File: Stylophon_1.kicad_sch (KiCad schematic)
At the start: 71 parts, among them J1 Conn_01x02_Socket, J2 +, J3 -, J4 Stylus, SW1 On/Off, SW2 Vibrato, T1 BC846, T2 BC846, U1 NE555D

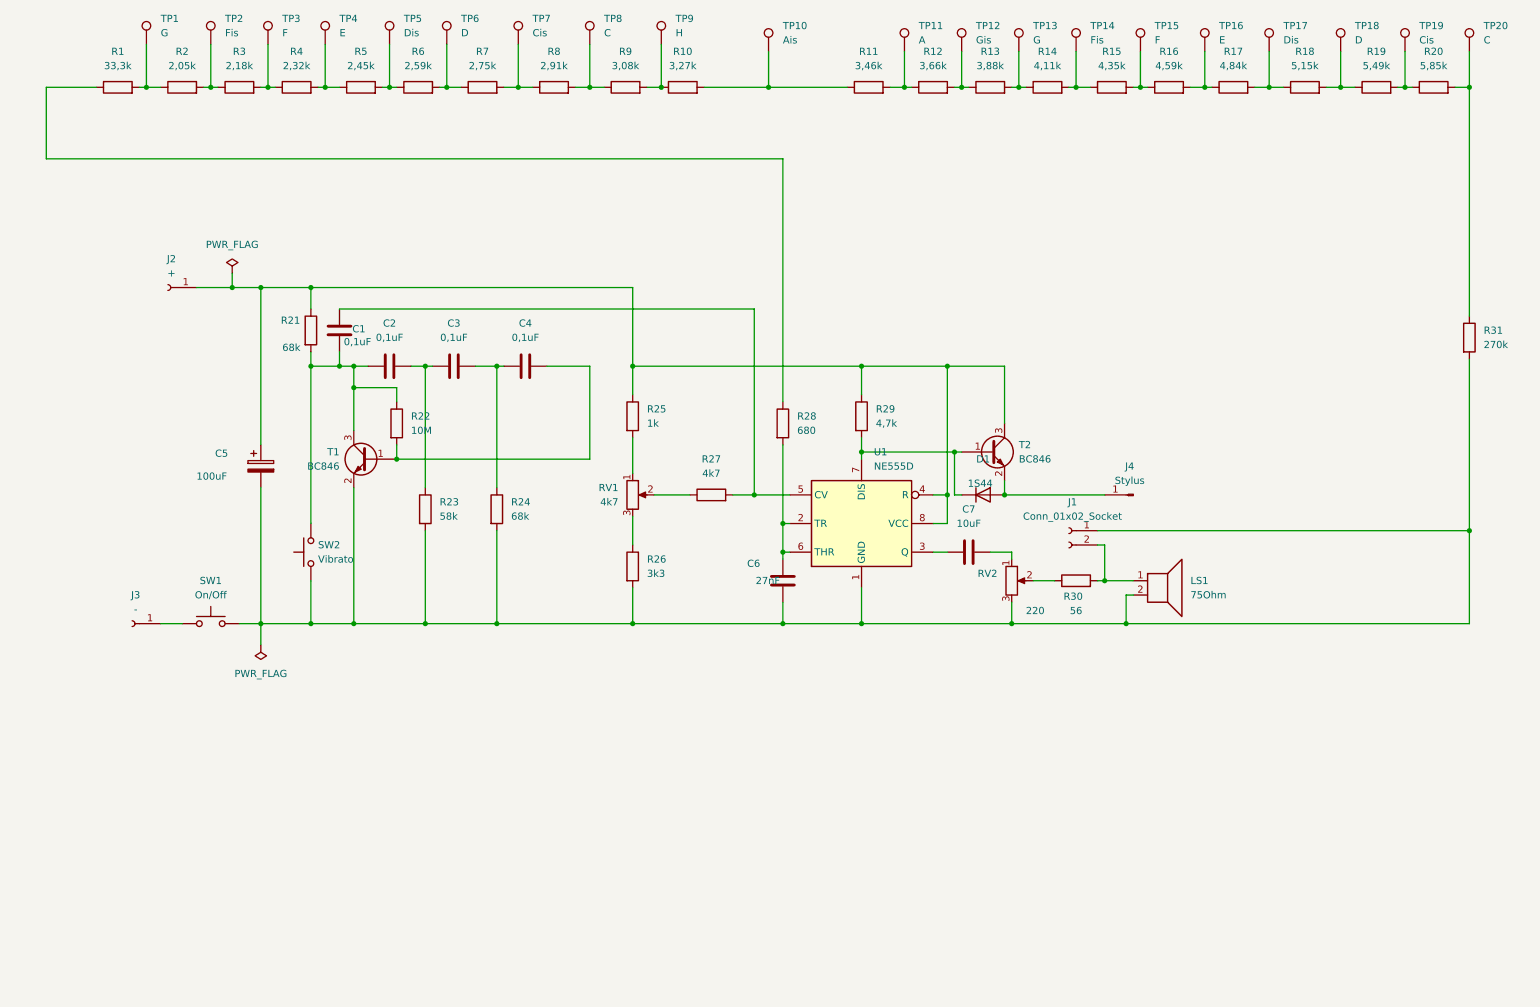
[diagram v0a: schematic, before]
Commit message: Updated Component Values
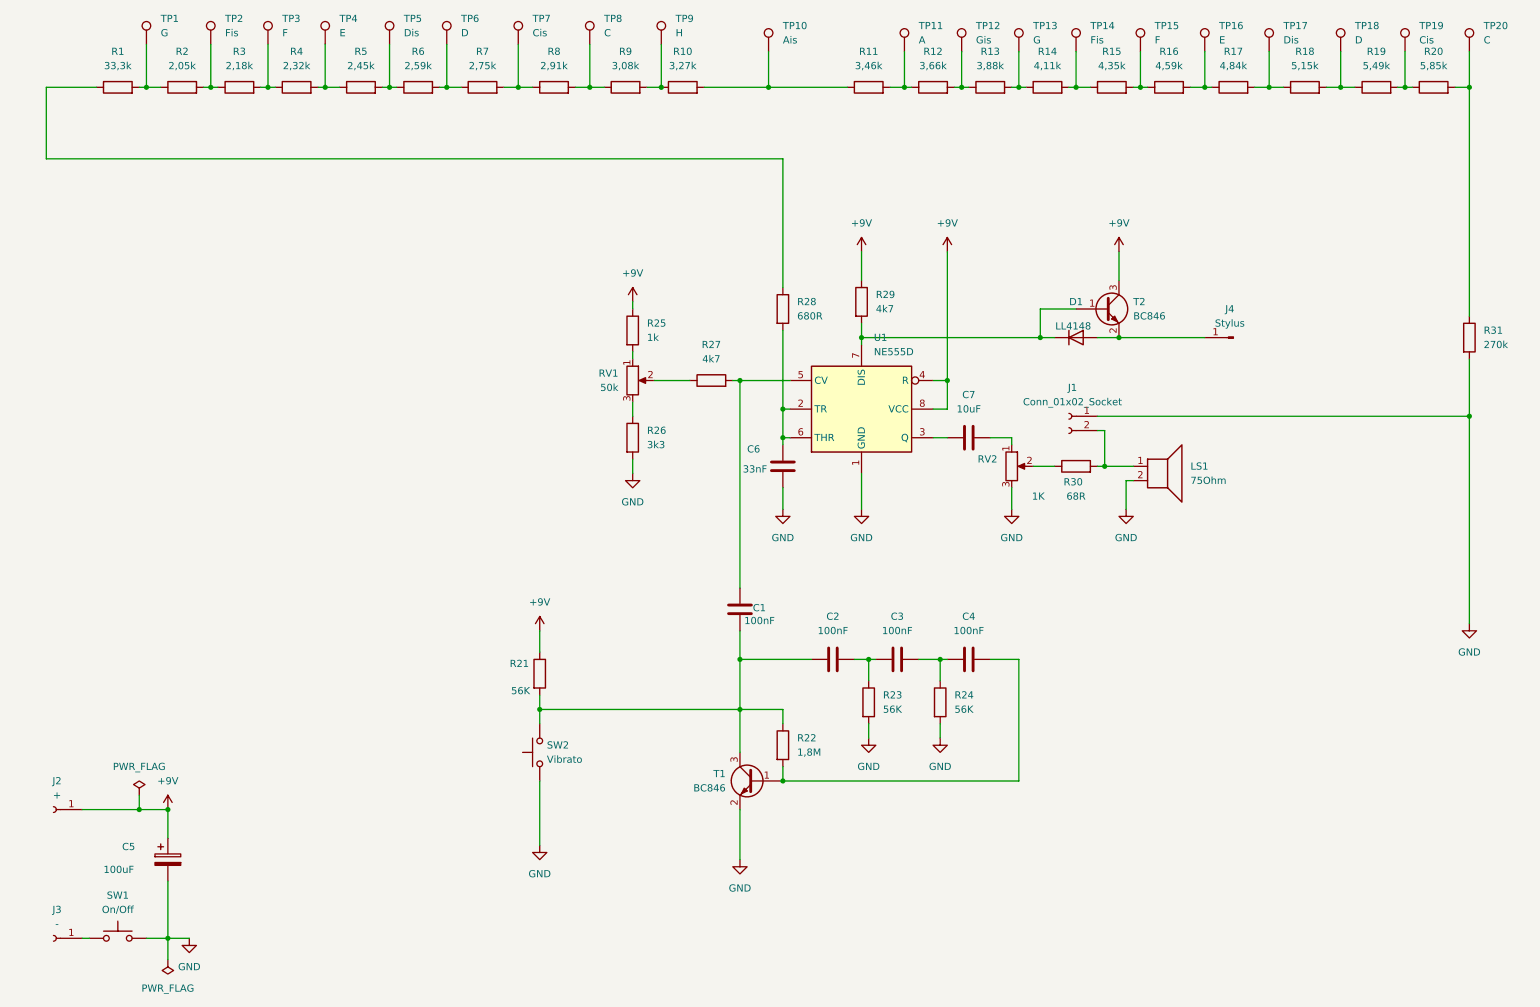
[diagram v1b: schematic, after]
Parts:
- C1, C2, C3, C4: value 0,1uF -> 100nF
- C6: value 27nF -> 33nF
- D1: value 1S44 -> LL4148
- R21, R24: value 68k -> 56K
- R22: value 10M -> 1,8M
- R23: value 58k -> 56K
- R28: value 680 -> 680R
- R29: value 4,7k -> 4k7
- R30: value 56 -> 68R
- RV1: value 4k7 -> 50k
- RV2: value 220 -> 1K
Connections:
- net +9V: now reaches C5.1, J2.1 (Pin_1), R21.1, R25.1, R29.1, T2.3 (C), U1.4 (R), U1.8 (VCC)
- net GND: now reaches C5.2, C6.2, J1.1 (Pin_1), LS1.2, R23.2, R24.2, R26.2, R31.2, RV2.3, SW1.2, SW2.1, T1.2 (E), U1.1 (GND)
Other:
- moved on the sheet: C1, C2, C3, C4, C5, C6, C7, D1, J1, J2, J3, J4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

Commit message: PCB updated
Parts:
- removed J2: +, Connector_PinHeader_2.00mm:PinHeader_1x01_P2.00mm_Vertical, symbol Connector:Conn_01x01_Socket
- removed J3: -, Connector_PinHeader_2.00mm:PinHeader_1x01_P2.00mm_Vertical, symbol Connector:Conn_01x01_Socket
- added BT1: Battery, Connector_PinHeader_2.54mm:PinHeader_1x02_P2.54mm_Vertical, symbol Device:Battery
- TP1, TP10, TP11, TP12, TP13, TP14, TP15, TP16, TP17, TP18, TP19, TP2, TP20, TP3, TP4, TP5, TP6, TP7, TP8, TP9: footprint TestPoint:TestPoint_Pad_4.0x4.0mm -> Keypads:Keypad_Small
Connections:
- net +9V: now also BT1.1 (+)
- net GND: now also LS1.1, RV2.1; no longer LS1.2, RV2.3
- net 5: now reaches R13.2, R14.1, TP13.1
- net 4,5: now reaches R14.2, R15.1, TP14.1
- net 6,5: now reaches R11.2, R12.1, TP11.1
- net 11: now reaches R3.2, R4.1, TP3.1
- net 10,5: now reaches R4.2, R5.1, TP4.1
- net 3,5: now reaches R16.2, R17.1, TP16.1
- net 6: now reaches R12.2, R13.1, TP12.1
- net 3: now reaches R17.2, R18.1, TP17.1
- net 2: now reaches R18.2, R19.1, TP18.1
- net 1: now reaches R20.2, R31.1, TP20.1
- net at SW1.1: now also BT1.2 (-)
- net 10: now reaches R5.2, R6.1, TP5.1
- net 8,5: now reaches R7.2, R8.1, TP7.1
- net 8: now reaches R8.2, R9.1, TP8.1
- net at C7.2: now also RV2.3; no longer RV2.1
- net at J1.2 (Pin_2), R30.2: now also LS1.2; no longer LS1.1
- net 7,5: now reaches R10.1, R9.2, TP9.1
- net 12: now reaches R1.2, R2.1, TP1.1
- net 11,5: now reaches R2.2, R3.1, TP2.1
- net 4: now reaches R15.2, R16.1, TP15.1
- net 7: now reaches R10.2, R11.1, TP10.1
- net 9: now reaches R6.2, R7.1, TP6.1
- net 1,5: now reaches R19.2, R20.1, TP19.1
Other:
- moved on the sheet: R10, R2, R3, TP2

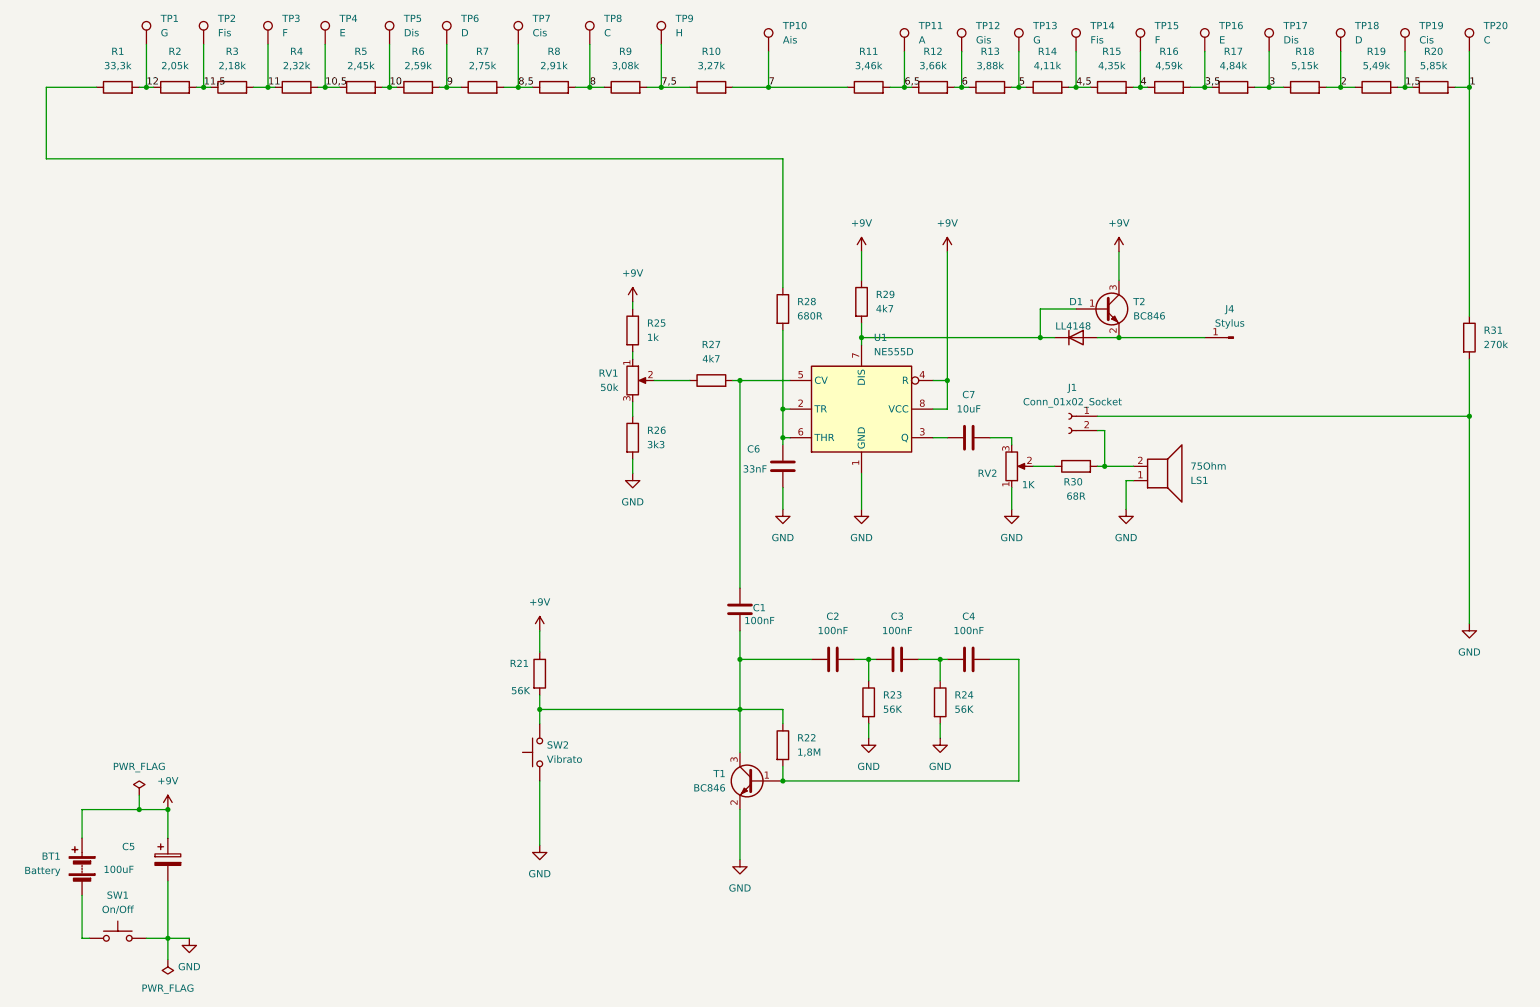
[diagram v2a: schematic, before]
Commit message: Added keys like a real one
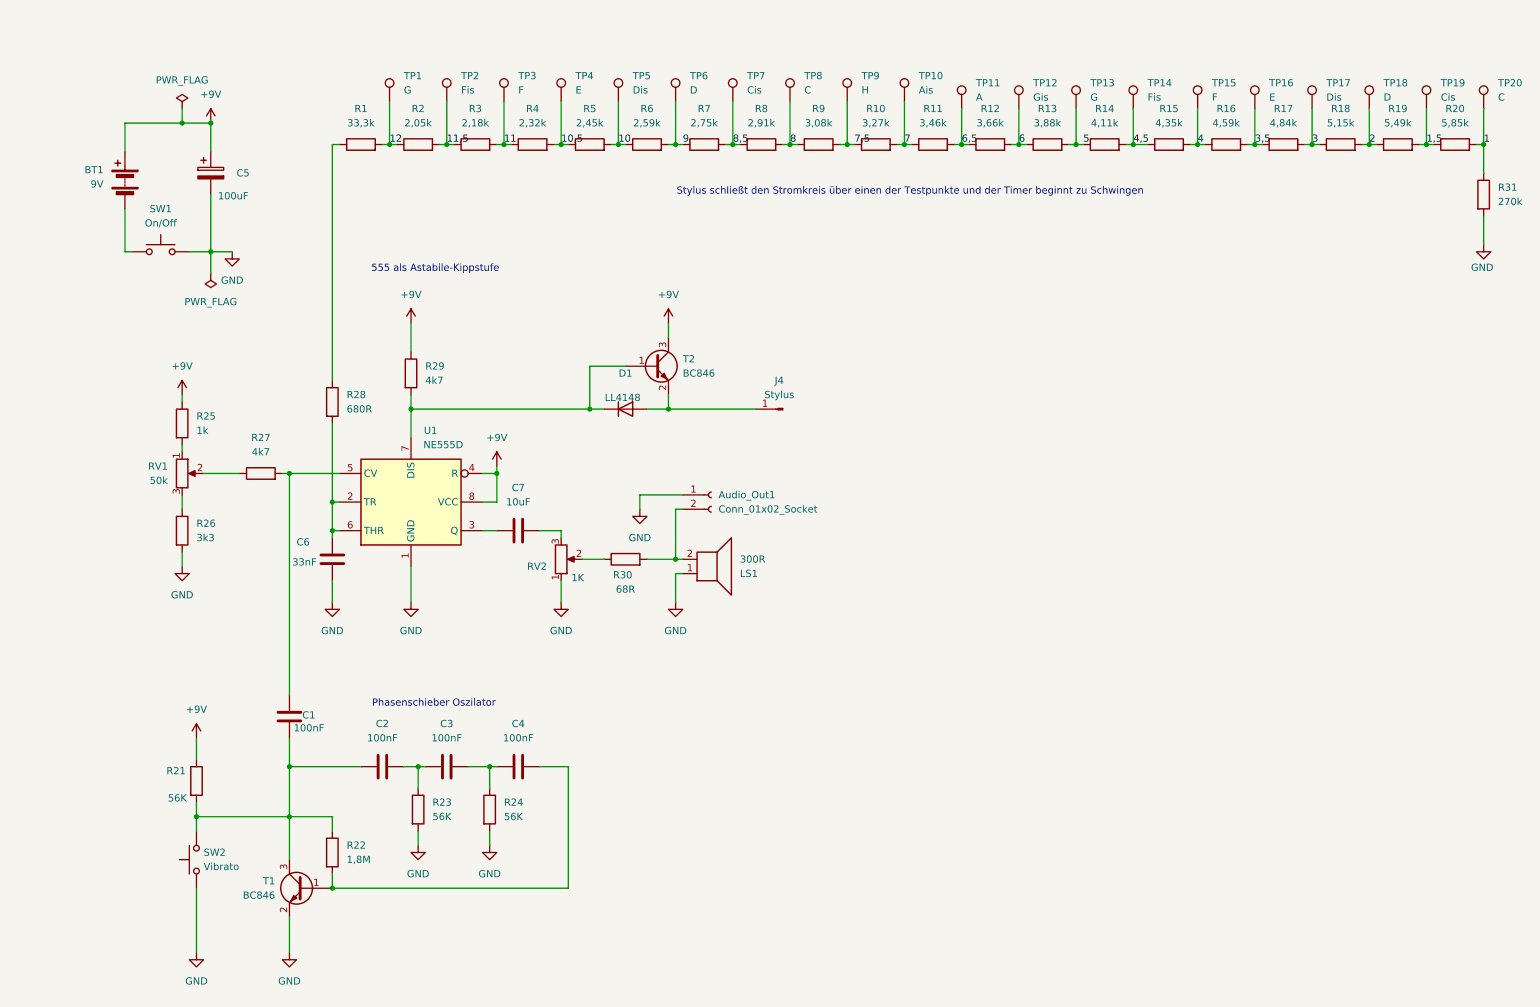
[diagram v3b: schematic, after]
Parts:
- BT1: value Battery -> 9V
- LS1: value 75Ohm -> 300R
- TP1, TP13, TP18, TP6: footprint Keypads:Keypad_Small -> Keypads:Keypad_Right; now left out of the parts list
- TP10, TP11, TP14, TP15, TP16, TP19, TP2, TP3, TP4, TP7, TP8, TP9: now left out of the parts list
- TP12, TP17, TP20, TP5: footprint Keypads:Keypad_Small -> Keypads:Keypad_Left; now left out of the parts list
- renumbered J1 to Audio_Out1
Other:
- note added: "555 als Astabile-Kippstufe"
- note added: "Phasenschieber Oszilator"
- note added: "Stylus schließt den Stromkreis über einen der Testpunkte und der Timer beginnt zu Schwingen"
- moved on the sheet: Audio_Out1, BT1, C1, C2, C3, C4, C5, C6, C7, D1, J4, LS1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

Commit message: VIA stitching & GND Plane QR
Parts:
- added TP21: 9V, TestPoint:TestPoint_Pad_D1.5mm, symbol Connector:TestPoint
- added TP22: GND, TestPoint:TestPoint_Pad_D1.5mm, symbol Connector:TestPoint
- added TP23: Output, TestPoint:TestPoint_Pad_D1.5mm, symbol Connector:TestPoint
- added TP24: Sinus, TestPoint:TestPoint_Pad_D1.5mm, symbol Connector:TestPoint
- added TP25: Batterie, TestPoint:TestPoint_Pad_D1.5mm, symbol Connector:TestPoint
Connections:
- net +9V: now also TP21.1, TP25.1
- net GND: now also TP22.1
- net at C1.1, C2.2, R21.2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: now also TP24.1
- net at C7.1, U1.3 (Q): now also TP23.1
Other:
- note added: "NE555 als Astabile-Kippstufe"
- note removed: "555 als Astabile-Kippstufe"

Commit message: title
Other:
- company: (none) -> HTL-Steyr
- title: (none) -> Stylophone
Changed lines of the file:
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@@
 	(generator_version "9.0")
 	(paper "A4")
+	(title_block
+		(title "Stylophone")
+		(date "2025-09-07")
+		(rev "1.0")
+		(company "HTL-Steyr")
+		(comment 1 "Gerrit Mitterhuemer")
+	)
 	(text "Phasenschieber Oszilator\n"
 		(exclude_from_sim no)

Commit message: Release V1.0
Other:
- note added: "Phasenschieber Oszilator für überlagerten Vibratoton"
- note removed: "Phasenschieber Oszilator"
- title: Stylophone -> Stiftklavier
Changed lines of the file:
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@@
 	(paper "A4")
 	(title_block
-		(title "Stylophone")
+		(title "Stiftklavier")
 		(date "2025-09-07")
 		(rev "1.0")
@@
 		(comment 1 "Gerrit Mitterhuemer")
 	)
-	(text "Phasenschieber Oszilator\n"
+	(text "Phasenschieber Oszilator für überlagerten Vibratoton\n"
 		(exclude_from_sim no)
 		(at 87.884 138.684 0)
